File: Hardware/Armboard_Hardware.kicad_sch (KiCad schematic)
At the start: 310 parts, among them J1 RJ45_LED_Shielded, Q1 SI4156DY, Q10 SI4156DY, Q11 SI4156DY, Q12 SI4156DY, Q13 SI4156DY, Q14 SI4156DY, Q15 SI4156DY, Q16 SI4156DY, Q17 SI4156DY, Q18 SI4156DY, Q19 SI4156DY, Q2 SI4156DY, Q20 SI4156DY, Q21 SI4156DY, Q22 SI4156DY, Q23 SI4156DY, Q24 SI4156DY, Q25 SI4156DY, Q26 SI4156DY, Q27 SI4156DY, Q28 SI4156DY, Q29 BSS138, Q3 SI4156DY, Q30 SI4156DY, Q31 SI4156DY, Q32 SI4156DY, Q33 SI4156DY, Q34 SI4156DY, Q35 SI4156DY, Q36 SI4156DY, Q37 SI4156DY, Q4 SI4156DY, Q5 SI4156DY, Q6 SI4156DY, Q7 SI4156DY, Q8 SI4156DY, Q9 SI4156DY, SW1 SW_Push, SW10 SW_SPDT, SW2 SW_Push, SW3 SW_Push, SW4 SW_Push, SW5 SW_Push, SW6 SW_Push, SW7 SW_Push, SW8 SW_Push, SW9 SW_Push, U1 Teensy4.1_DEV-16771, U10 IRS2005S, U11 IRS2005S, U12 IRS2005S, U13 IRS2005S, U14 OKI, U15 IRS2005S, U16 IRS2005S, U17 IRS2005S, U18 IRS2005S, U19 IRS2005S, U2 IRS2005S, U20 IRS2005S, U21 74LVC2G04, U22 74LVC2G04, U23 74LVC2G04, U24 74LVC2G04, U25 74LVC2G04, U26 74LVC2G04, U27 74LVC2G04, U28 74LVC2G04, U29 74LVC2G04, U3 IRS2005S, U30 74HC148, U31 74HC148, U32 74HC00, U4 IRS2005S, U5 IRS2005S, U6 IRS2005S, U7 IRS2005S, U8 IRS2005S, U9 IRS2005S

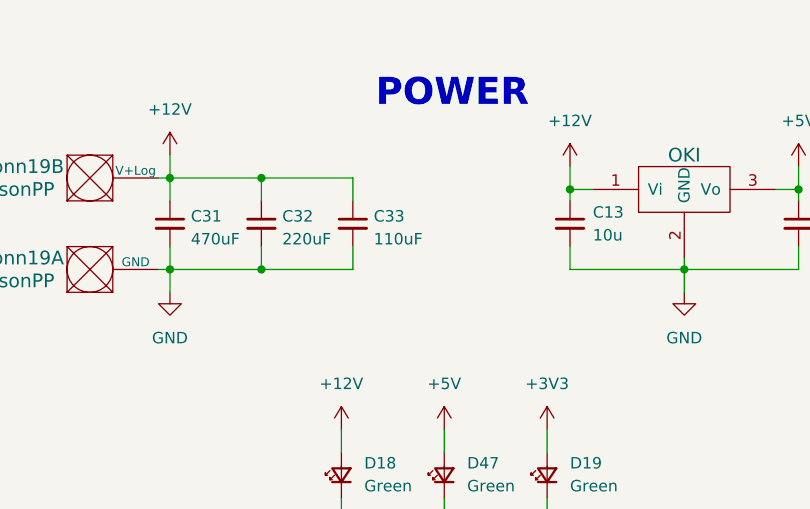
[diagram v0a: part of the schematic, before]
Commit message: Fixed incorrect capacitor value
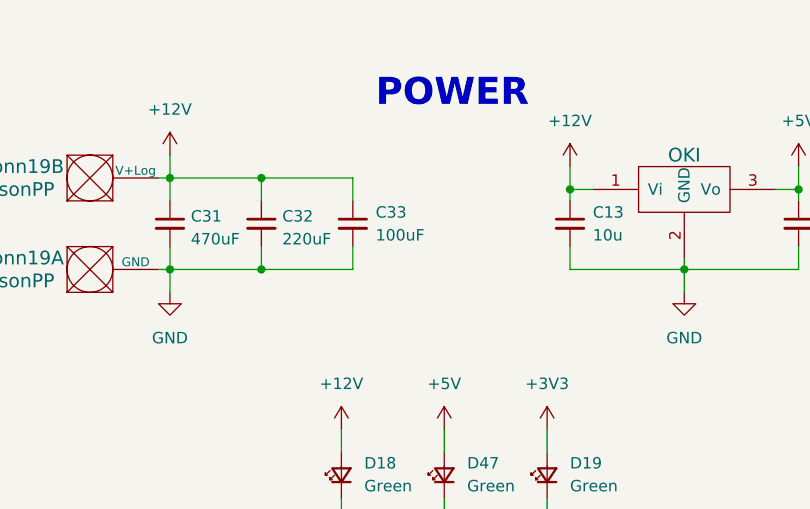
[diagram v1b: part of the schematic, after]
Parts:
- C33: value 110uF -> 100uF
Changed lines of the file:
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@@
   (symbol (lib_id "Device:C_Small") (at 261.62 34.29 0) (unit 1)
     (in_bom yes) (on_board yes) (fields_autoplaced)
-    (property "Reference" "C33" (id 0) (at 263.9441 33.4616 0)
+    (property "Reference" "C33" (id 0) (at 264.16 33.0262 0)
       (effects (font (size 1.27 1.27)) (justify left))
     )
-    (property "Value" "110uF" (id 1) (at 263.9441 35.9985 0)
+    (property "Value" "100uF" (id 1) (at 264.16 35.5662 0)
       (effects (font (size 1.27 1.27)) (justify left))
     )
@@
     )
     (path "/24f915cc-0dd1-4959-afb4-a0936df5df72"
-      (reference "C33") (unit 1) (value "110uF") (footprint "Capacitor_THT:CP_Radial_D6.3mm_P2.50mm")
+      (reference "C33") (unit 1) (value "100uF") (footprint "Capacitor_THT:CP_Radial_D6.3mm_P2.50mm")
     )
     (path "/a811d801-e3b3-484a-8487-8894e49c61cb"
